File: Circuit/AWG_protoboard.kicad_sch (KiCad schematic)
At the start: 12 parts, among them J1 Power, J2 Pump 1, J3 Pump 2, J4 Mosfet, J5 Arduino, M1 Fan_3pin, M2 Fan_3pin, U2 LCD-016N002L

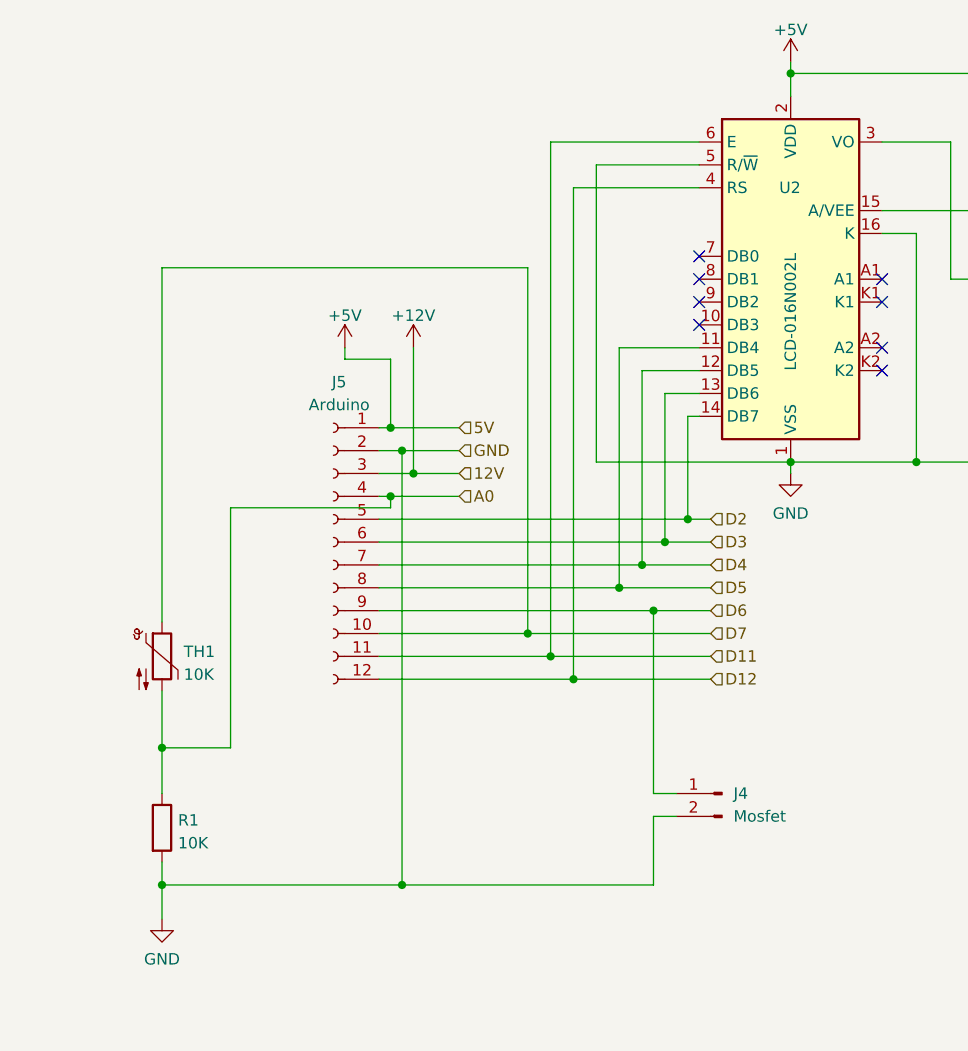
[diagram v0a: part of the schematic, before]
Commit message: [Circuit] Improvements on protoboard layout
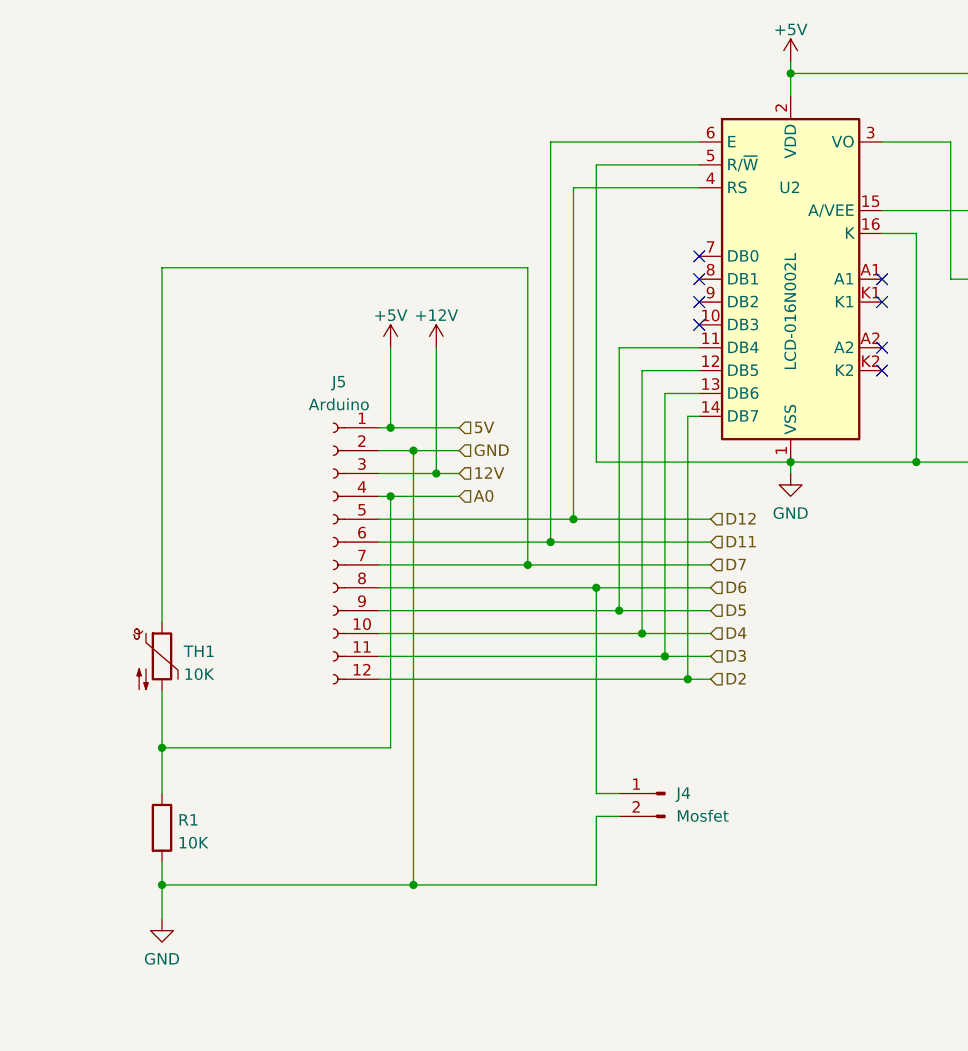
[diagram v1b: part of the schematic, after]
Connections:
- net D11: now also J5.6 (Pin_6); no longer J5.11 (Pin_11)
- net D12: now also J5.5 (Pin_5); no longer J5.12 (Pin_12)
- net D2: now also J5.12 (Pin_12); no longer J5.5 (Pin_5)
- net D3: now also J5.11 (Pin_11); no longer J5.6 (Pin_6)
- net D4: now also J5.10 (Pin_10); no longer J5.7 (Pin_7)
- net D5: now also J5.9 (Pin_9); no longer J5.8 (Pin_8)
- net D6: now also J5.8 (Pin_8); no longer J5.9 (Pin_9)
- net D7: now also J5.7 (Pin_7); no longer J5.10 (Pin_10)
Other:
- moved on the sheet: J4
